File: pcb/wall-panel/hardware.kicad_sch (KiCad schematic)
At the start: 4 parts

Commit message: wall panel v0.3
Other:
- company: Grigorii Merkushev (aka brushknight) -> dotstar.tech
- title: Wall panel -> Wall Panel
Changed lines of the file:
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@@
 	(paper "A3")
 	(title_block
-		(title "Wall panel")
-		(date "2026-01-09")
-		(rev "1")
-		(company "Grigorii Merkushev (aka brushknight)")
-		(comment 1 "brushknight.com")
+		(title "Wall Panel")
+		(date "2026-02-02")
+		(rev "v0.3")
+		(company "dotstar.tech")
+		(comment 1 "designed by Grigorii Merkushev (aka brushknight)")
+		(comment 2 "brushknight.com")
 	)
 	(no_connect
@@
 		)
 		(instances
-			(project "CM4IOv5"
+			(project "wall_panel"
 				(path "/e63e39d7-6ac0-4ffd-8aa3-1841a4541b55/2a110465-dd07-4872-9dc5-b05104e43751"
 					(reference "H4")
@@
 		)
 		(instances
-			(project "CM4IOv5"
+			(project "wall_panel"
 				(path "/e63e39d7-6ac0-4ffd-8aa3-1841a4541b55/2a110465-dd07-4872-9dc5-b05104e43751"
 					(reference "H2")
@@
 		)
 		(instances
-			(project "CM4IOv5"
+			(project "wall_panel"
 				(path "/e63e39d7-6ac0-4ffd-8aa3-1841a4541b55/2a110465-dd07-4872-9dc5-b05104e43751"
 					(reference "H3")

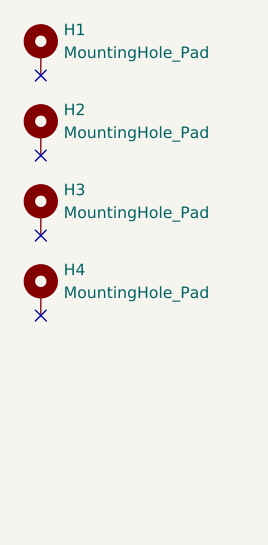
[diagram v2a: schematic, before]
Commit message: pogo pins wall panel
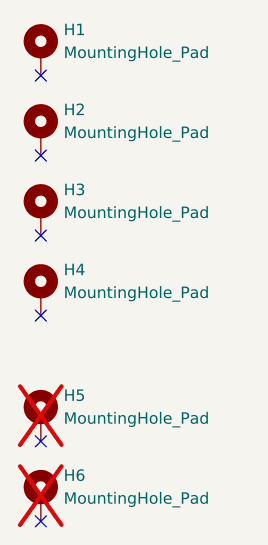
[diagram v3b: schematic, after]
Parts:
- added H5, H6: MountingHole_Pad, 9774030151R:9774030151R, symbol Mechanical:MountingHole_Pad
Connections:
- no-connect marks 4 -> 6
